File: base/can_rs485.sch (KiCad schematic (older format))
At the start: 4 parts

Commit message: Update base board: 1. Add extra analog voltage input to core board.   -> update pinmux 2. Assign most footprints. 3. Generate netlist. 4. Add core_sf board. 5. Add kicad_symbols library submodule.
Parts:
- D29: renamed from D?; footprint TO_SOT_Packages_SMD:SOT-23 -> Package_TO_SOT_SMD:SOT-23
- gave numbers to parts that had none: 3
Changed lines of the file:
@@
 +5V
 $Comp
-L SN65HVD230 U?
+L SN65HVD230 U21
 U 1 1 5A3C3395
 P 2000 2500
-F 0 "U?" H 1900 2900 50  0000 R CNN
+F 0 "U21" H 1900 2900 50  0000 R CNN
 F 1 "SN65HVD230" H 1900 2800 50  0000 R CNN
 F 2 "Package_SOIC:SOIC-8_3.9x4.9mm_P1.27mm" H 2000 2000 50  0001 C CNN
@@
 	2400 2600 3500 2600
 $Comp
-L C C?
+L C C41
 U 1 1 5A3C342C
 P 1500 1150
-F 0 "C?" H 1525 1250 50  0000 L CNN
+F 0 "C41" H 1525 1250 50  0000 L CNN
 F 1 "0.1uF" H 1525 1050 50  0000 L CNN
 F 2 "Capacitor_SMD:C_0603_1608Metric" H 1538 1000 50  0001 C CNN
@@
 GNDD
 $Comp
-L +3.3V #PWR?
+L +3.3V #PWR027
 U 1 1 5A3C351C
 P 1700 900
-F 0 "#PWR?" H 1700 750 50  0001 C CNN
+F 0 "#PWR027" H 1700 750 50  0001 C CNN
 F 1 "+3.3V" H 1700 1040 50  0000 C CNN
 F 2 "" H 1700 900 50  0001 C CNN
@@
 $EndComp
 $Comp
-L GND #PWR?
+L GND #PWR028
 U 1 1 5A3C3534
 P 1700 1400
-F 0 "#PWR?" H 1700 1150 50  0001 C CNN
+F 0 "#PWR028" H 1700 1150 50  0001 C CNN
 F 1 "GND" H 1700 1250 50  0000 C CNN
 F 2 "" H 1700 1400 50  0001 C CNN
@@
 $EndComp
 $Comp
-L GND #PWR?
+L GND #PWR029
 U 1 1 5A3C354C
 P 2000 3000
-F 0 "#PWR?" H 2000 2750 50  0001 C CNN
+F 0 "#PWR029" H 2000 2750 50  0001 C CNN
 F 1 "GND" H 2000 2850 50  0000 C CNN
 F 2 "" H 2000 3000 50  0001 C CNN
@@
 	2000 3000 2000 2900
 $Comp
-L +3.3V #PWR?
+L +3.3V #PWR030
 U 1 1 5A3C3569
 P 2000 2100
-F 0 "#PWR?" H 2000 1950 50  0001 C CNN
+F 0 "#PWR030" H 2000 1950 50  0001 C CNN
 F 1 "+3.3V" H 2000 2240 50  0000 C CNN
 F 2 "" H 2000 2100 50  0001 C CNN
@@
 	2000 2200 2000 2100
 $Comp
-L R R?
+L R R43
 U 1 1 5A3C3843
 P 1400 2950
-F 0 "R?" V 1480 2950 50  0000 C CNN
+F 0 "R43" V 1480 2950 50  0000 C CNN
 F 1 "100" V 1400 2950 50  0000 C CNN
 F 2 "Resistor_SMD:R_0603_1608Metric" V 1330 2950 50  0001 C CNN
@@
 	1400 3100 1400 3200
 $Comp
-L GND #PWR?
+L GND #PWR031
 U 1 1 5A3C38B7
 P 1400 3200
-F 0 "#PWR?" H 1400 2950 50  0001 C CNN
+F 0 "#PWR031" H 1400 2950 50  0001 C CNN
 F 1 "GND" H 1400 3050 50  0000 C CNN
 F 2 "" H 1400 3200 50  0001 C CNN
@@
 	1400 2500 1600 2500
 $Comp
-L NUP2105L D?
+L NUP2105L D29
 U 1 1 5A3C4E77
 P 2700 2900
-F 0 "D?" H 2925 3000 50  0000 L CNN
+F 0 "D29" H 2925 3000 50  0000 L CNN
 F 1 "NUP2105L" H 2925 2925 50  0000 L CNN
-F 2 "TO_SOT_Packages_SMD:SOT-23" H 2925 2850 50  0001 L CNN
+F 2 "Package_TO_SOT_SMD:SOT-23" H 2925 2850 50  0001 L CNN
 F 3 "" H 2825 3025 50  0001 C CNN
 	1    2700 2900
@@
 	2700 3100 2700 3200
 $Comp
-L GND #PWR?
+L GND #PWR032
 U 1 1 5A3C4FCE
 P 2700 3200
-F 0 "#PWR?" H 2700 2950 50  0001 C CNN
+F 0 "#PWR032" H 2700 2950 50  0001 C CNN
 F 1 "GND" H 2700 3050 50  0000 C CNN
 F 2 "" H 2700 3200 50  0001 C CNN

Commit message: temp-sens-fan was created
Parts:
- added C?: 0.1uF, Capacitor_SMD:C_0603_1608Metric, symbol C
- added JP?: Jumper_NC_Small, symbol Jumper_NC_Small
- added R?: 120, Connector_PinHeader_2.54mm:PinHeader_1x02_P2.54mm_Vertical, symbol R
- added U?: MAX485CSA, Package_SOIC:SO-8_5.3x6.2mm_P1.27mm, symbol MAX485E
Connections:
- net +5V: now also C?.1, U?.8 (VCC)
- net GND: now also C?.2, U?.5 (GND)
- net RS485+: now also R?.1, U?.6 (A)
- net RS485-: now also JP?.1, U?.7 (B)
- net RS485_RX: now also U?.4 (DI)
- net RS485_TX: now also U?.1 (RO)
- net RS485_TXEN: now also U?.2 (~RE), U?.3 (DE)
- new net: JP?.2, R?.2
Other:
- moved on the sheet: D29
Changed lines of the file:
@@
 LIBS:texas
 LIBS:opto
+LIBS:maxim
 LIBS:4hbd-base-cache
 EELAYER 25 0
@@
 Text HLabel 3500 2600 2    60   BiDi ~ 0
 CAN_L
-Text HLabel 5400 3500 0    60   BiDi ~ 0
+Text HLabel 4550 5600 2    60   BiDi ~ 0
 RS485+
-Text HLabel 5400 3600 0    60   BiDi ~ 0
+Text HLabel 4550 5300 2    60   BiDi ~ 0
 RS485-
-Text HLabel 6900 3250 0    60   Input ~ 0
+Text HLabel 2350 5300 0    60   Input ~ 0
 RS485_TX
-Text HLabel 6900 3350 0    60   Input ~ 0
+Text HLabel 2350 5450 0    60   Input ~ 0
 RS485_TXEN
-Text HLabel 6900 3450 0    60   Output ~ 0
+Text HLabel 2450 5600 0    60   Output ~ 0
 RS485_RX
-Text HLabel 6900 3700 0    60   Input ~ 0
+Text HLabel 1250 4600 0    60   Input ~ 0
 +5V
 $Comp
@@
 L NUP2105L D29
 U 1 1 5A3C4E77
-P 2700 2900
-F 0 "D29" H 2925 3000 50  0000 L CNN
-F 1 "NUP2105L" H 2925 2925 50  0000 L CNN
-F 2 "Package_TO_SOT_SMD:SOT-23" H 2925 2850 50  0001 L CNN
-F 3 "" H 2825 3025 50  0001 C CNN
-	1    2700 2900
-	1    0    0    -1
-$EndComp
-Wire Wire Line
-	2800 2700 2800 2500
+P 2700 3100
+F 0 "D29" H 2925 3200 50  0000 L CNN
+F 1 "NUP2105L" H 2925 3125 50  0000 L CNN
+F 2 "Package_TO_SOT_SMD:SOT-23" H 2925 3050 50  0001 L CNN
+F 3 "" H 2825 3225 50  0001 C CNN
+	1    2700 3100
+	1    0    0    -1
+$EndComp
+Wire Wire Line
+	2800 2500 2800 2900
 Connection ~ 2800 2500
 Wire Wire Line
-	2600 2700 2600 2600
+	2600 2600 2600 2900
 Connection ~ 2600 2600
 Wire Wire Line
-	2700 3100 2700 3200
+	2700 3300 2700 3400
 $Comp
 L GND #PWR032
 U 1 1 5A3C4FCE
-P 2700 3200
-F 0 "#PWR032" H 2700 2950 50  0001 C CNN
-F 1 "GND" H 2700 3050 50  0000 C CNN
-F 2 "" H 2700 3200 50  0001 C CNN
-F 3 "" H 2700 3200 50  0001 C CNN
-	1    2700 3200
-	1    0    0    -1
-$EndComp
+P 2700 3400
+F 0 "#PWR032" H 2700 3150 50  0001 C CNN
+F 1 "GND" H 2700 3250 50  0000 C CNN
+F 2 "" H 2700 3400 50  0001 C CNN
+F 3 "" H 2700 3400 50  0001 C CNN
+	1    2700 3400
+	1    0    0    -1
+$EndComp
+$Comp
+L MAX485E U?
+U 1 1 5A44C7B1
+P 3250 5400
+F 0 "U?" H 3010 5850 50  0000 C CNN
+F 1 "MAX485CSA" H 3280 5850 50  0000 L CNN
+F 2 "Package_SOIC:SO-8_5.3x6.2mm_P1.27mm" H 3250 4700 50  0001 C CNN
+F 3 "" H 3250 5450 50  0001 C CNN
+	1    3250 5400
+	1    0    0    -1
+$EndComp
+Wire Wire Line
+	2850 5400 2750 5400
+Wire Wire Line
+	2750 5400 2750 5500
+Wire Wire Line
+	2750 5500 2850 5500
+Wire Wire Line
+	2350 5450 2750 5450
+Connection ~ 2750 5450
+Wire Wire Line
+	2350 5300 2850 5300
+Wire Wire Line
+	2450 5600 2850 5600
+Wire Wire Line
+	4550 5300 3650 5300
+Wire Wire Line
+	4550 5600 3650 5600
+Wire Wire Line
+	1250 4600 3250 4600
+Wire Wire Line
+	3250 4600 3250 4900
+$Comp
+L GND #PWR033
+U 1 1 5A44CCE9
+P 3250 6150
+F 0 "#PWR033" H 3250 5900 50  0001 C CNN
+F 1 "GND" H 3250 6000 50  0000 C CNN
+F 2 "" H 3250 6150 50  0001 C CNN
+F 3 "" H 3250 6150 50  0001 C CNN
+	1    3250 6150
+	1    0    0    -1
+$EndComp
+Wire Wire Line
+	3250 6000 3250 6150
+$Comp
+L C C?
+U 1 1 5A44D127
+P 1450 4850
+F 0 "C?" H 1475 4950 50  0000 L CNN
+F 1 "0.1uF" H 1475 4750 50  0000 L CNN
+F 2 "Capacitor_SMD:C_0603_1608Metric" H 1488 4700 50  0001 C CNN
+F 3 "" H 1450 4850 50  0001 C CNN
+	1    1450 4850
+	1    0    0    -1
+$EndComp
+Wire Wire Line
+	1450 6050 3250 6050
+Connection ~ 3250 6050
+Wire Wire Line
+	1450 4700 1450 4600
+Connection ~ 1450 4600
+Wire Wire Line
+	1450 6050 1450 5000
+$Comp
+L Jumper_NC_Small JP?
+U 1 1 5A44DA0F
+P 3950 5450
+F 0 "JP?" H 3950 5530 50  0000 C CNN
+F 1 "Jumper_NC_Small" H 3960 5390 50  0001 C CNN
+F 2 "" H 3950 5450 50  0001 C CNN
+F 3 "" H 3950 5450 50  0001 C CNN
+	1    3950 5450
+	1    0    0    -1
+$EndComp
+$Comp
+L R R?
+U 1 1 5A44DAB5
+P 4250 5450
+F 0 "R?" V 4330 5450 50  0000 C CNN
+F 1 "120" V 4250 5450 50  0000 C CNN
+F 2 "Connector_PinHeader_2.54mm:PinHeader_1x02_P2.54mm_Vertical" V 4180 5450 50  0001 C CNN
+F 3 "" H 4250 5450 50  0001 C CNN
+	1    4250 5450
+	0    1    1    0
+$EndComp
+Wire Wire Line
+	4400 5450 4450 5450
+Wire Wire Line
+	4450 5450 4450 5600
+Connection ~ 4450 5600
+Wire Wire Line
+	4100 5450 4050 5450
+Wire Wire Line
+	3850 5450 3800 5450
+Wire Wire Line
+	3800 5450 3800 5300
+Connection ~ 3800 5300
 $EndSCHEMATC

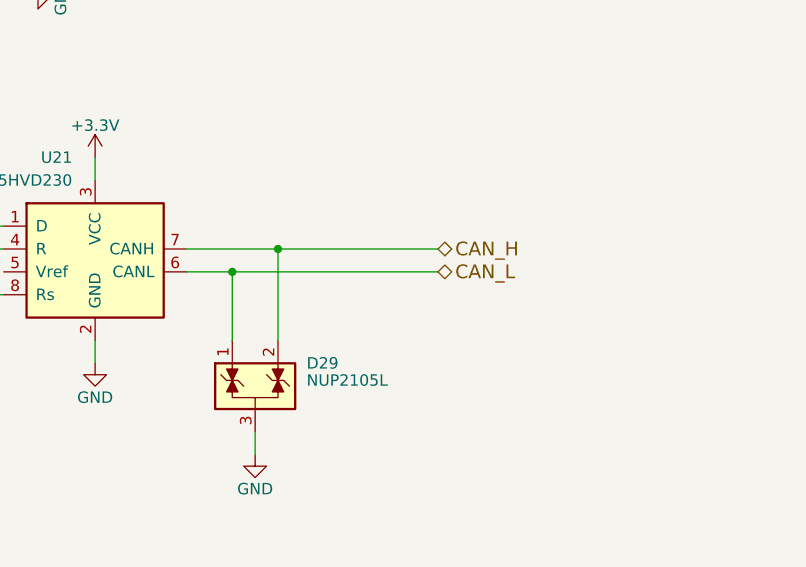
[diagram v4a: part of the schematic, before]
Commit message: Update footprints.
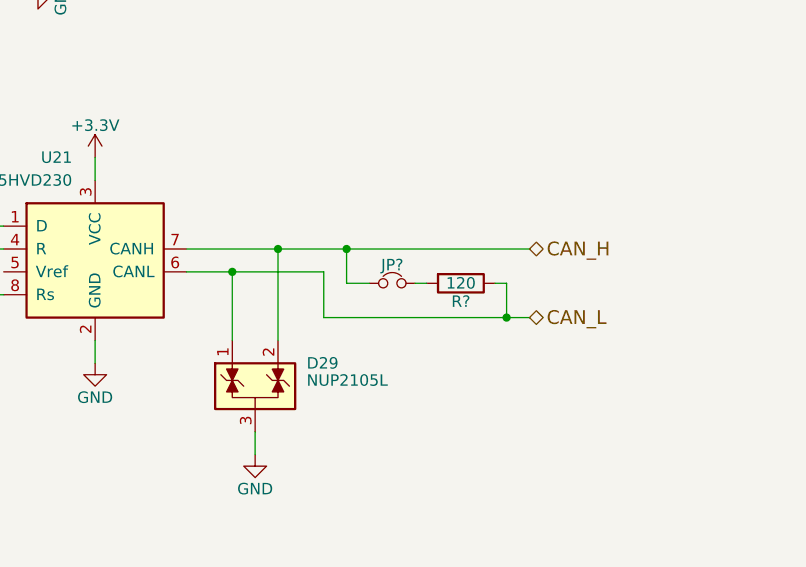
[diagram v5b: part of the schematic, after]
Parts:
- added JP?: Jumper_NC_Small, Connector_PinHeader_2.54mm:PinHeader_1x02_P2.54mm_Vertical, symbol Jumper_NC_Small
- added R?: 120, Resistor_SMD:R_0603_1608Metric, symbol R
- JP?: footprint (none) -> Connector_PinHeader_2.54mm:PinHeader_1x02_P2.54mm_Vertical
- R?: footprint Connector_PinHeader_2.54mm:PinHeader_1x02_P2.54mm_Vertical -> Resistor_SMD:R_0603_1608Metric
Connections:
- net CAN_H: now also JP?.1
- net CAN_L: now also R?.1
- new net: JP?.2, R?.2
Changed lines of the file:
@@
 Comment4 ""
 $EndDescr
-Text HLabel 3500 2500 2    60   BiDi ~ 0
+Text HLabel 3900 2500 2    60   BiDi ~ 0
 CAN_H
-Text HLabel 3500 2600 2    60   BiDi ~ 0
+Text HLabel 3900 2800 2    60   BiDi ~ 0
 CAN_L
 Text HLabel 4550 5600 2    60   BiDi ~ 0
@@
 $EndComp
 Wire Wire Line
-	2400 2500 3500 2500
-Wire Wire Line
-	2400 2600 3500 2600
+	2400 2500 3900 2500
 $Comp
 L C C41
@@
 F 0 "JP?" H 3950 5530 50  0000 C CNN
 F 1 "Jumper_NC_Small" H 3960 5390 50  0001 C CNN
-F 2 "" H 3950 5450 50  0001 C CNN
+F 2 "Connector_PinHeader_2.54mm:PinHeader_1x02_P2.54mm_Vertical" H 3950 5450 50  0001 C CNN
 F 3 "" H 3950 5450 50  0001 C CNN
 	1    3950 5450
@@
 F 0 "R?" V 4330 5450 50  0000 C CNN
 F 1 "120" V 4250 5450 50  0000 C CNN
-F 2 "Connector_PinHeader_2.54mm:PinHeader_1x02_P2.54mm_Vertical" V 4180 5450 50  0001 C CNN
+F 2 "Resistor_SMD:R_0603_1608Metric" V 4180 5450 50  0001 C CNN
 F 3 "" H 4250 5450 50  0001 C CNN
 	1    4250 5450
@@
 	3800 5450 3800 5300
 Connection ~ 3800 5300
+$Comp
+L Jumper_NC_Small JP?
+U 1 1 5A450646
+P 3300 2650
+F 0 "JP?" H 3300 2730 50  0000 C CNN
+F 1 "Jumper_NC_Small" H 3310 2590 50  0001 C CNN
+F 2 "Connector_PinHeader_2.54mm:PinHeader_1x02_P2.54mm_Vertical" H 3300 2650 50  0001 C CNN
+F 3 "" H 3300 2650 50  0001 C CNN
+	1    3300 2650
+	1    0    0    -1
+$EndComp
+$Comp
+L R R?
+U 1 1 5A45064C
+P 3600 2650
+F 0 "R?" V 3680 2650 50  0000 C CNN
+F 1 "120" V 3600 2650 50  0000 C CNN
+F 2 "Resistor_SMD:R_0603_1608Metric" V 3530 2650 50  0001 C CNN
+F 3 "" H 3600 2650 50  0001 C CNN
+	1    3600 2650
+	0    1    1    0
+$EndComp
+Wire Wire Line
+	3750 2650 3800 2650
+Wire Wire Line
+	3800 2650 3800 2800
+Wire Wire Line
+	3450 2650 3400 2650
+Wire Wire Line
+	2400 2600 3000 2600
+Wire Wire Line
+	3000 2600 3000 2800
+Wire Wire Line
+	3000 2800 3900 2800
+Connection ~ 3800 2800
+Wire Wire Line
+	3200 2650 3100 2650
+Wire Wire Line
+	3100 2650 3100 2500
+Connection ~ 3100 2500
 $EndSCHEMATC

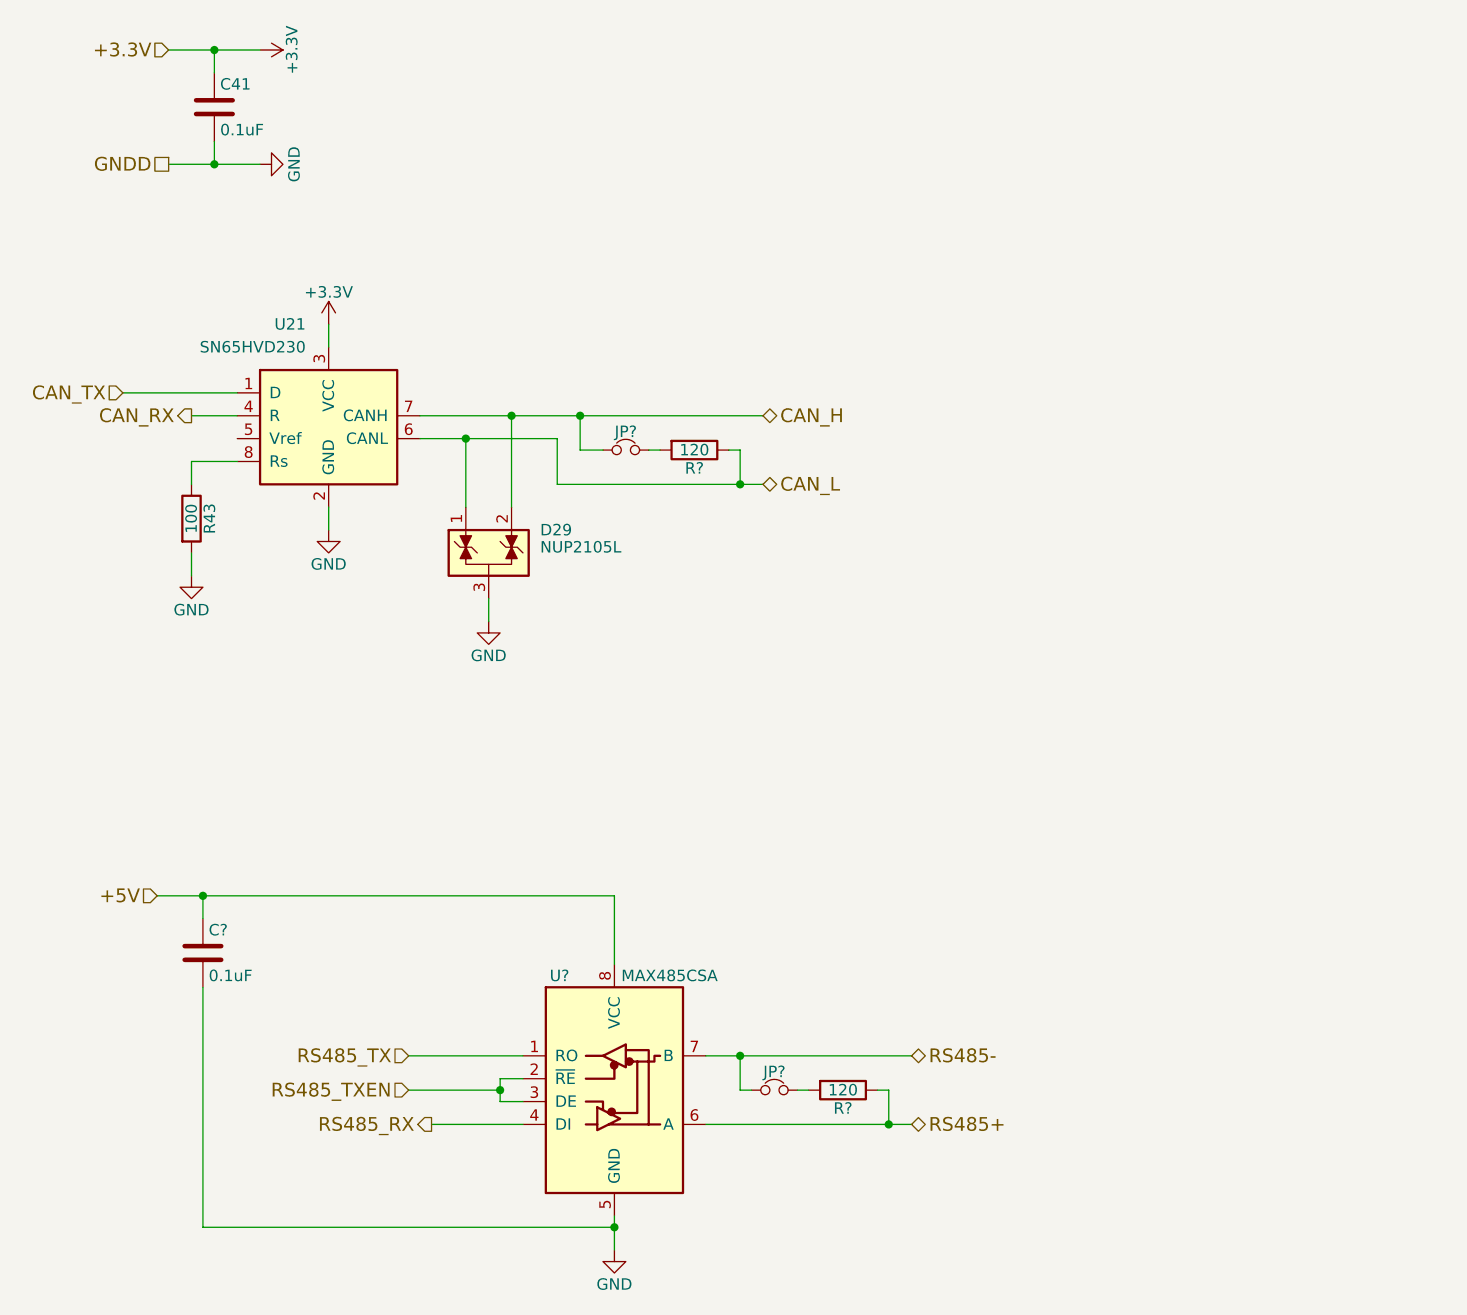
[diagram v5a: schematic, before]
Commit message: A few updates to test points.
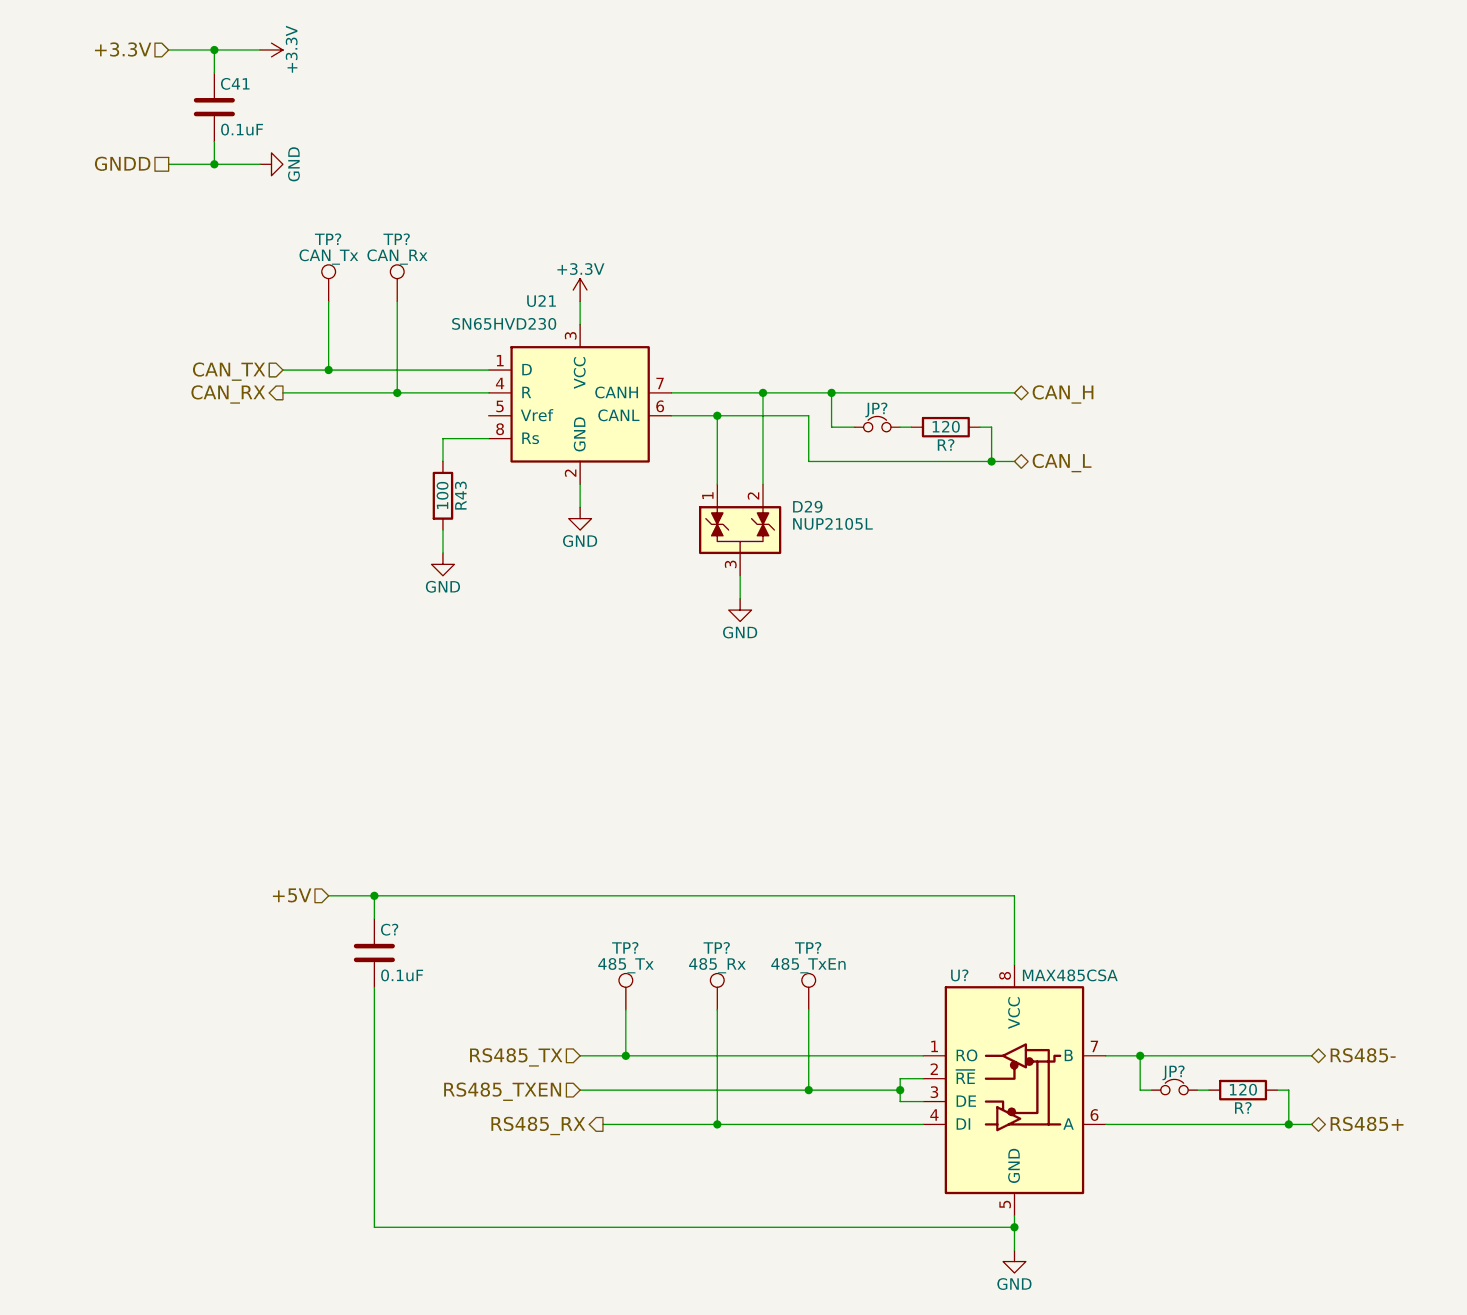
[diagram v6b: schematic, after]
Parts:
- added TP?: CAN_Tx, symbol Test_Point
- added TP?: CAN_Rx, symbol Test_Point
- added TP?: 485_Tx, symbol Test_Point
- added TP?: 485_Rx, symbol Test_Point
- added TP?: 485_TxEn, symbol Test_Point
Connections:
- net CAN_RX: now also TP?.1
- net CAN_TX: now also TP?.1
- net RS485_RX: now also TP?.1
- net RS485_TX: now also TP?.1
- net RS485_TXEN: now also TP?.1
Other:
- moved on the sheet: C?, D29, JP?, R43, R?, U21, U?
